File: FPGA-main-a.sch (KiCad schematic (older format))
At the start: 27 parts, among them U1 XC7A75T-FTG256

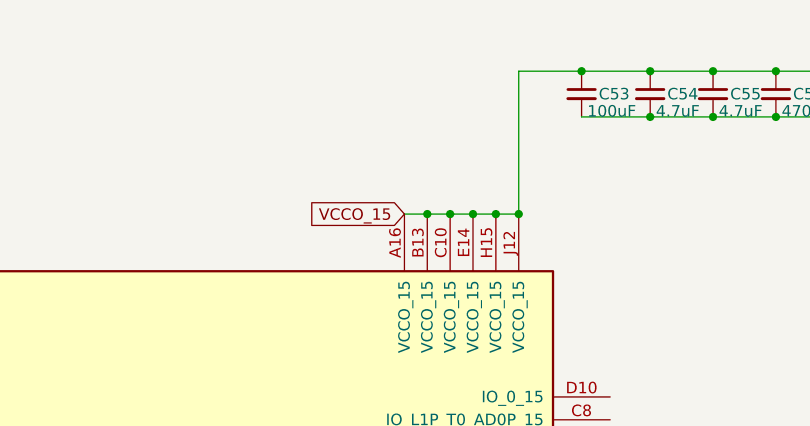
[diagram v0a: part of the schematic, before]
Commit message: Add power plane setup
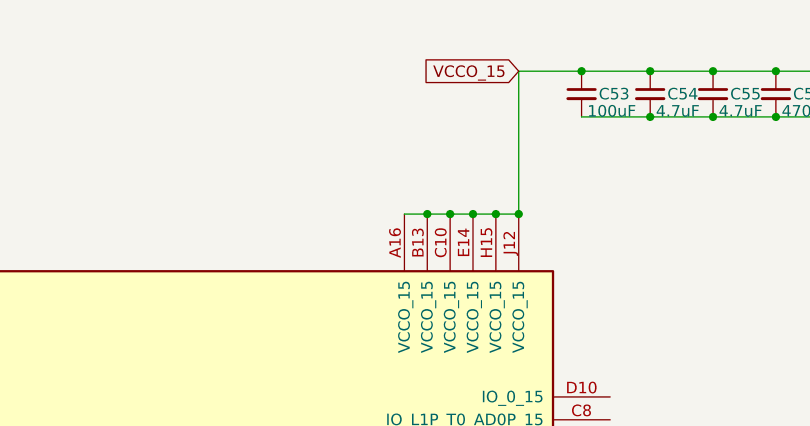
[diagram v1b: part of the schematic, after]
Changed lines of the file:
@@
 	-1   0    0    -1
 $EndComp
-Text GLabel 9475 3125 0    50   Input ~ 0
+Text GLabel 9975 2500 0    50   Input ~ 0
 VCCO_15
 $Comp

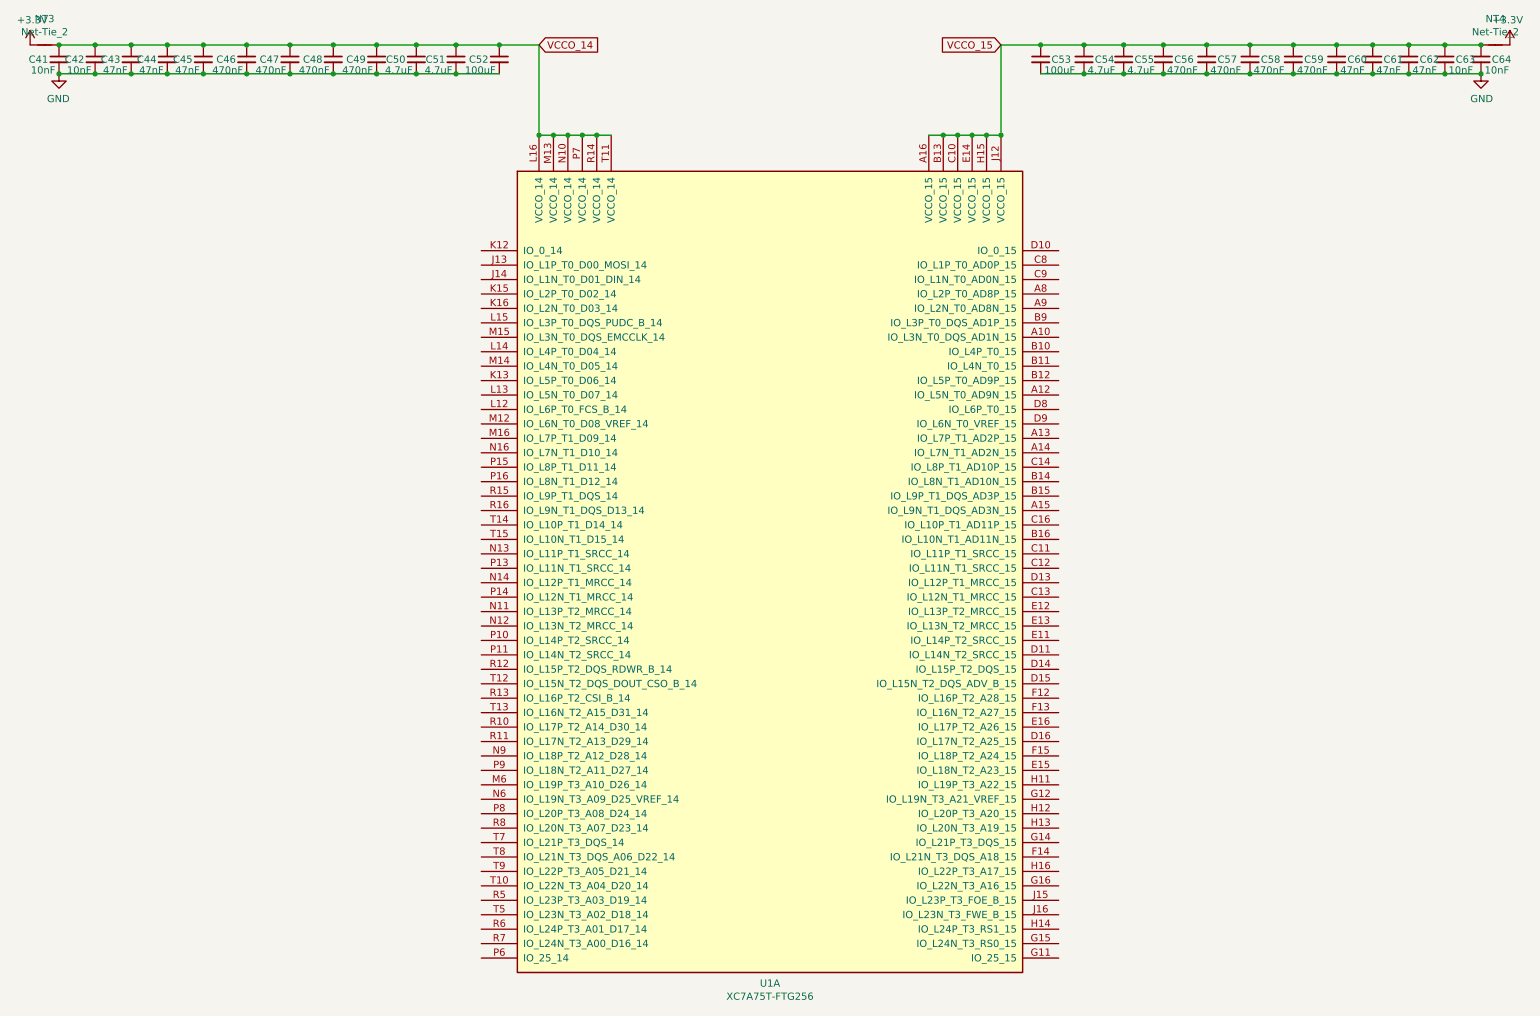
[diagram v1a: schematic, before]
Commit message: Add wire up for Q-SPI flash module.
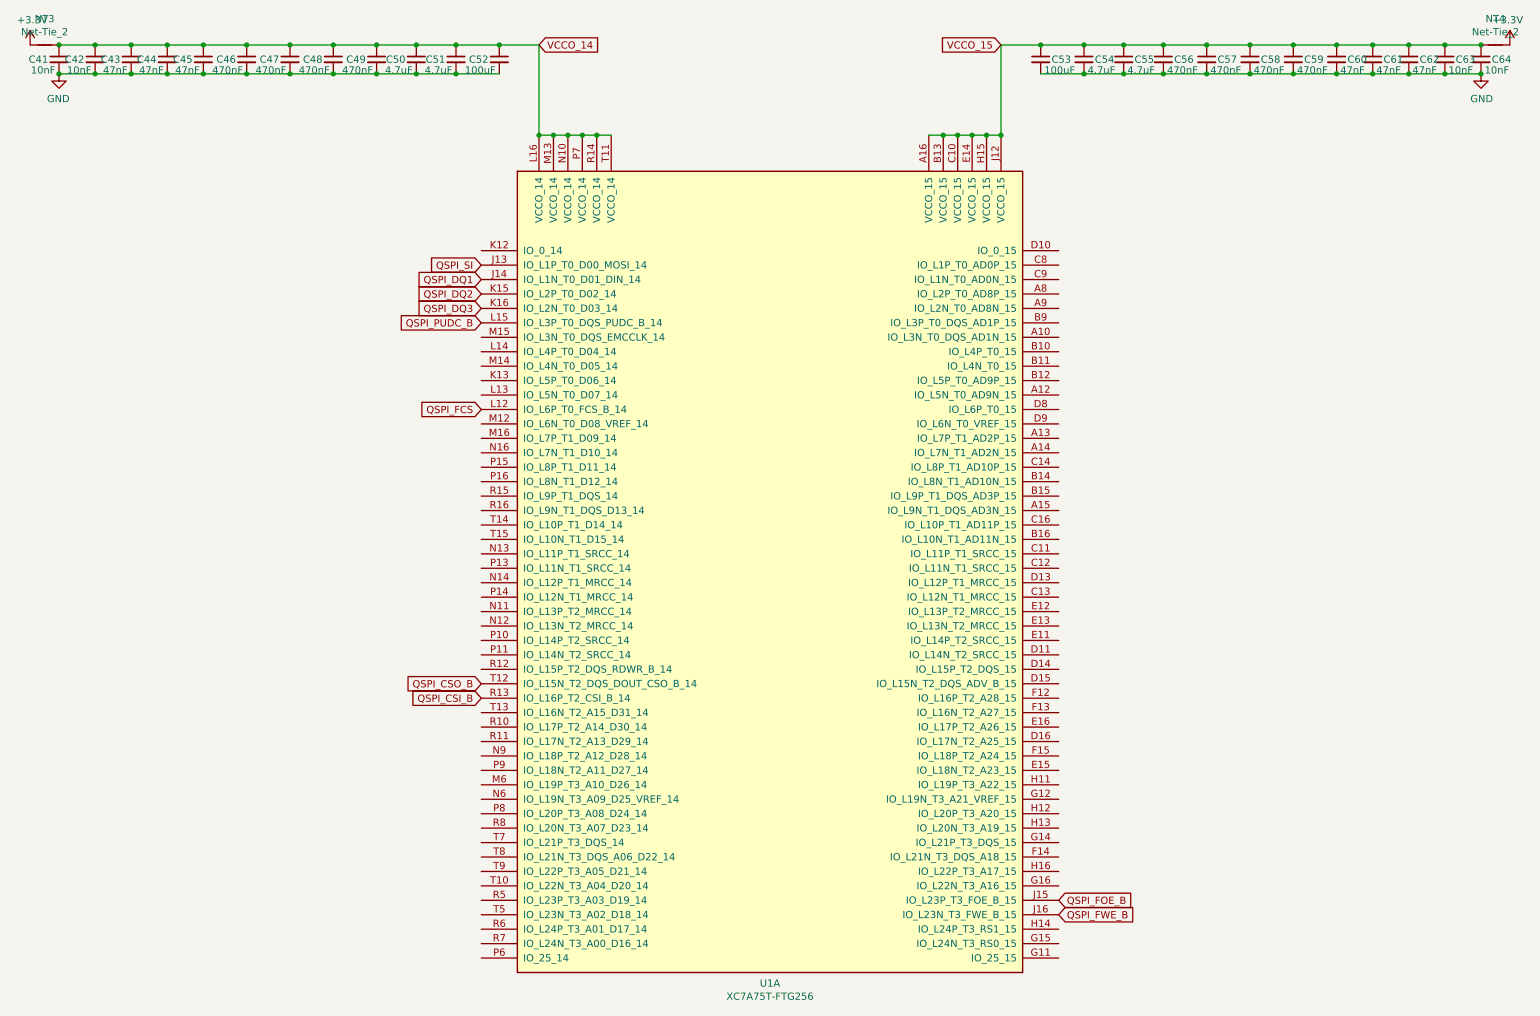
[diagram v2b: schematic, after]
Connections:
- net QSPI_SI: now reaches U1.J13 (IO_L1P_T0_D00_MOSI_14)
- net QSPI_DQ1: now reaches U1.J14 (IO_L1N_T0_D01_DIN_14)
- net QSPI_FOE_B: now reaches U1.J15 (IO_L23P_T3_FOE_B_15)
- net QSPI_FWE_B: now reaches U1.J16 (IO_L23N_T3_FWE_B_15)
- net QSPI_DQ2: now reaches U1.K15 (IO_L2P_T0_D02_14)
- net QSPI_DQ3: now reaches U1.K16 (IO_L2N_T0_D03_14)
- net QSPI_FCS: now reaches U1.L12 (IO_L6P_T0_FCS_B_14)
- net QSPI_PUDC_B: now reaches U1.L15 (IO_L3P_T0_DQS_PUDC_B_14)
- net QSPI_CSI_B: now reaches U1.R13 (IO_L16P_T2_CSI_B_14)
- net QSPI_CSO_B: now reaches U1.T12 (IO_L15N_T2_DQS_DOUT_CSO_B_14)
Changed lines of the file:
@@
 Text GLabel 6775 2500 2    50   Input ~ 0
 VCCO_14
+Text GLabel 6375 5025 0    50   Input ~ 0
+QSPI_FCS
+Text GLabel 10375 8425 2    50   Input ~ 0
+QSPI_FOE_B
+Text GLabel 10375 8525 2    50   Input ~ 0
+QSPI_FWE_B
+Text GLabel 6375 6925 0    50   Input ~ 0
+QSPI_CSO_B
+Text GLabel 6375 7025 0    50   Input ~ 0
+QSPI_CSI_B
+Text GLabel 6375 4425 0    50   Input ~ 0
+QSPI_PUDC_B
+Text GLabel 6375 4225 0    50   Input ~ 0
+QSPI_DQ2
+Text GLabel 6375 4325 0    50   Input ~ 0
+QSPI_DQ3
+Text GLabel 6375 4125 0    50   Input ~ 0
+QSPI_DQ1
+Text GLabel 6375 4025 0    50   Input ~ 0
+QSPI_SI
 $EndSCHEMATC
